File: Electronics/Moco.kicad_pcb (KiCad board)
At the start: 2 copper layers, 34 x 34 mm, 51 parts, among them J1 Conn_01x04, J2 Conn_01x01, J3 Conn_ARM_JTAG_SWD_10, J4 Conn_01x03, J5 Conn_01x01, J6 Conn_01x04, J8 Conn_01x01, J9 Conn_01x01, U1 EFM32PG22C200FxxIM32, U2 SP485EN, U3 TMAG5273, U4 DRV8311, Y1 ECS-384-CDX-1983

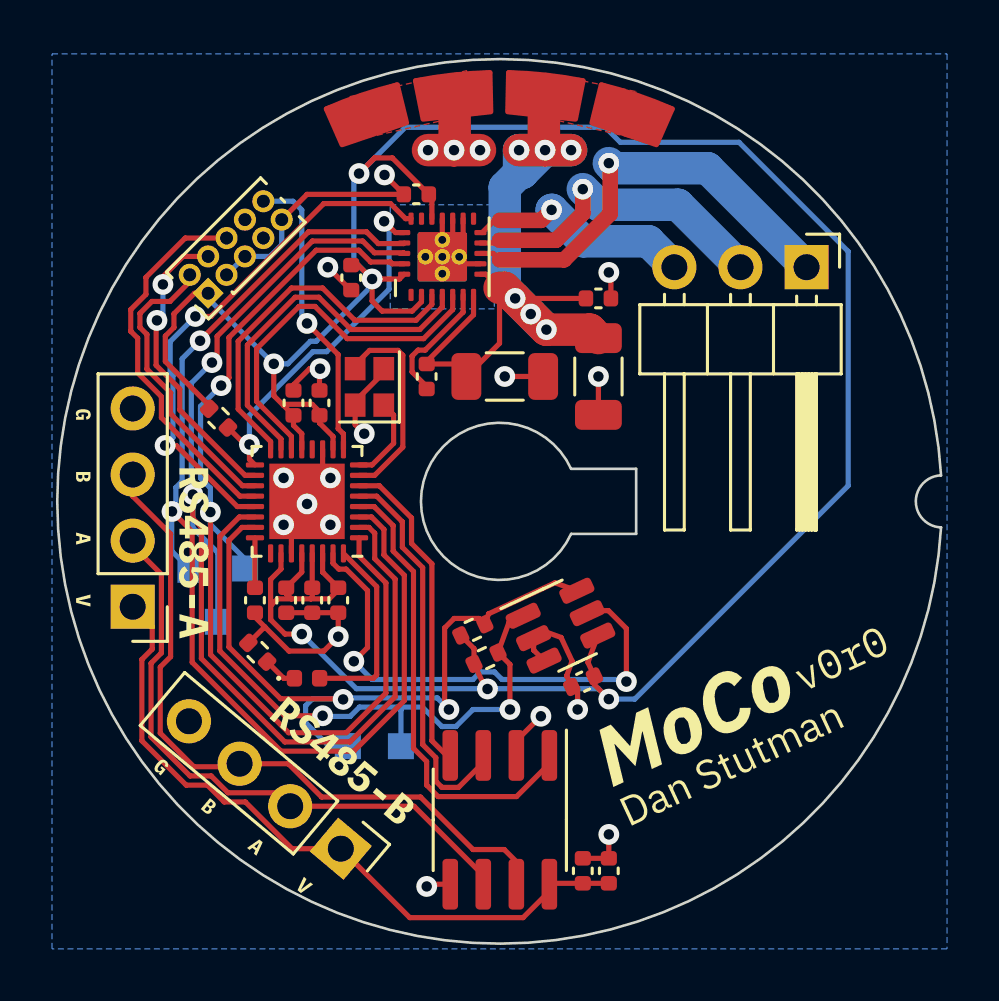
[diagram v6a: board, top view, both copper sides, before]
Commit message: New design with ESP32-C3
This design swaps the EFM32PG22 for an ESP32-C3. This reduces cost
and improves availability. It also lets me use USB and CANbus instead
of RS485.
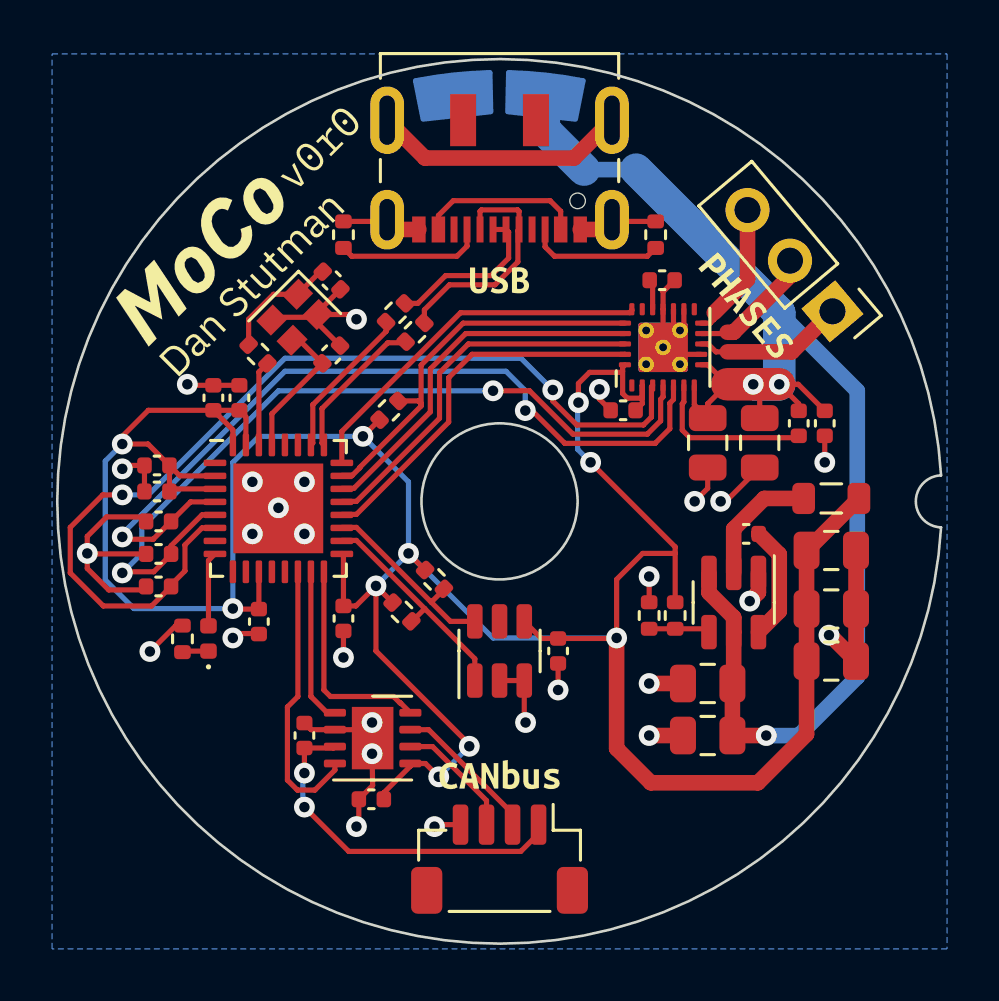
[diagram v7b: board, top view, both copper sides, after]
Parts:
- removed C16: 0.1 + 2.7 uF 6.3V X5R, Capacitor_SMD:C_0402_1005Metric
- removed C2, C3: 0.1 uF 6.3V X5R, Capacitor_SMD:C_0402_1005Metric
- removed C4: 0.1 + 1 uF 6.3V X5R, Capacitor_SMD:C_0402_1005Metric
- removed C6: 0.01 + 1 uF 6.3V X5R, Capacitor_SMD:C_0402_1005Metric
- removed J1: Conn_01x04, Connector_PinHeader_2.54mm:PinHeader_1x04_P2.54mm_Vertical
- removed J2, J5: Conn_01x01, Library:Pad_CircularEdge_Ro16.5Ri15_Single
- removed TP1, TP2, TP3, TP4, TP5: TestPoint, TestPoint:TestPoint_Pad_1.0x1.0mm
- removed kibuzzard-624C45BD: G***, kibuzzard-624C45BD
- removed kibuzzard-624C45C7: G***, kibuzzard-624C45C7
- removed kibuzzard-624C45D0: G***, kibuzzard-624C45D0
- removed kibuzzard-624C45D8: G***, kibuzzard-624C45D8
- removed kibuzzard-624C45E2: G***, kibuzzard-624C45E2
- removed kibuzzard-6257E5BB: G***, kibuzzard-6257E5BB
- removed kibuzzard-6257E5C8: G***, kibuzzard-6257E5C8
- removed kibuzzard-6257E666 (x2): G***, kibuzzard-6257E666
- added C14: C_Small, Capacitor_SMD:C_0402_1005Metric, F.Cu at (36.9, 50.8)
- added C17: C_Small, Capacitor_SMD:C_0402_1005Metric, F.Cu at (36.9, 52.0)
- added C18: C_Small, Capacitor_SMD:C_0402_1005Metric, F.Cu at (40.0, 46.0)
- added C19: C_Small, Capacitor_SMD:C_0402_1005Metric, F.Cu at (43.5, 44.4)
- added C20: C_Small, Capacitor_SMD:C_0402_1005Metric, F.Cu at (43.5, 41.5)
- added C21: C_Small, Capacitor_SMD:C_0402_1005Metric, F.Cu at (36.8, 48.6)
- added C22: C_Small, Capacitor_SMD:C_0402_1005Metric, F.Cu at (36.8, 49.6)
- added C23: C_Small, Capacitor_SMD:C_0402_1005Metric, F.Cu at (40.8, 54.6)
- added C24: C_Small, Capacitor_SMD:C_0402_1005Metric, F.Cu at (44.0, 54.5)
- added C25: C_Small, Capacitor_SMD:C_0402_1005Metric, F.Cu at (36.9, 53.3)
- added C26: 10uF, Capacitor_SMD:C_0805_2012Metric, F.Cu at (58.0, 57.0)
- added C27: 10uF, Capacitor_SMD:C_0805_2012Metric, F.Cu at (58.0, 59.0)
- added C28: 0.1uF, Capacitor_SMD:C_0402_1005Metric, F.Cu at (59.5, 51.2)
- added C29: 22uF, Capacitor_SMD:C_0805_2012Metric, F.Cu at (62.8, 51.9)
- added C30: 22uF, Capacitor_SMD:C_0805_2012Metric, F.Cu at (62.8, 54.1)
- added C31: 22uF, Capacitor_SMD:C_0805_2012Metric, F.Cu at (62.8, 56.1)
- added L2: 3.3uH 114mR, Inductor_SMD:L_0805_2012Metric, F.Cu at (62.8, 49.9)
- added R10: 22R, Resistor_SMD:R_0402_1005Metric, F.Cu at (46.8, 43.5)
- added R11: 22R, Resistor_SMD:R_0402_1005Metric, F.Cu at (46.0, 42.8)
- added R5: R_Small_US, Resistor_SMD:R_0402_1005Metric, F.Cu at (40.7, 44.3)
- added R6: 33.2kR, Resistor_SMD:R_0402_1005Metric, F.Cu at (56.8, 54.4)
- added R7: 10kR, Resistor_SMD:R_0402_1005Metric, F.Cu at (55.8, 54.4)
- added R8: 5.1kR, Resistor_SMD:R_0402_1005Metric, F.Cu at (56.0, 39.8)
- added R9: 5.1kR, Resistor_SMD:R_0402_1005Metric, F.Cu at (44.0, 39.8)
- added U5: TJA1462ATK/0Z, Package_SON:HVSON-8-1EP_3x3mm_P0.65mm_EP1.6x2.4mm, F.Cu at (45.1, 59.1)
- added kibuzzard-626ED451: G***, kibuzzard-626ED451, F.Cu at (50.0, 60.5)
- added kibuzzard-626ED465: G***, kibuzzard-626ED465, F.Cu at (50.0, 41.5)
- added kibuzzard-626ED487: G***, kibuzzard-626ED487, F.Cu at (59.5, 42.5)
- C1: value 1 uF 6.3V X5R -> C_Small
- C12: value 1uF 6.3V X7R -> 0.1uF 6.3V X7R
- C13, C15: footprint Capacitor_SMD:C_1206_3216Metric -> Capacitor_SMD:C_0805_2012Metric
- J3: value Conn_ARM_JTAG_SWD_10 -> USB_C_Receptacle_USB2.0; footprint Connector_PinHeader_1.00mm:PinHeader_2x05_P1.00mm_Vertical -> Connector_USB:USB_C_Receptacle_JAE_DX07S016JA1R1500
- J4: footprint Connector_PinHeader_2.54mm:PinHeader_1x03_P2.54mm_Horizontal -> Connector_PinHeader_2.54mm:PinHeader_1x03_P2.54mm_Vertical
- J6: footprint Connector_PinHeader_2.54mm:PinHeader_1x04_P2.54mm_Vertical -> Connector_JST:JST_SH_BM04B-SRSS-TB_1x04-1MP_P1.00mm_Vertical
- J8, J9: moved to B.Cu
- R1, R2: value 910kR -> 910R
- U1: value EFM32PG22C200FxxIM32 -> ESP32-C3; footprint Package_DFN_QFN:QFN-32-1EP_4x4mm_P0.4mm_EP2.9x2.9mm -> Package_DFN_QFN:QFN-32-1EP_5x5mm_P0.5mm_EP3.45x3.45mm
- U2: value SP485EN -> TPS562201; footprint Package_SO:SOIC-8_3.9x4.9mm_P1.27mm -> Package_TO_SOT_SMD:SOT-23-6
- Y1: value ECS-384-CDX-1983 -> XTAL
- moved kibuzzard-624C491C 28.1 mm to (43.1, 36.4), turned to 45 degrees
- moved kibuzzard-6244D452 26.1 mm to (40.5, 41.6), turned to 45 degrees
- moved kibuzzard-6244CA09 26.0 mm to (38.5, 40.5), turned to 45 degrees
- moved C8 14.4 mm to (61.5, 47.0)
- moved J3 12.5 mm to (50.0, 36.5), turned to 180 degrees
- moved U2 12.3 mm to (59.0, 53.9)
- moved C5 11.9 mm to (42.5, 59.0)
- moved C7 11.6 mm to (54.8, 46.5), turned to 0 degrees
- moved C10 10.0 mm to (56.2, 41.5), turned to 0 degrees
- moved C11 9.94 mm to (62.5, 47.0), turned to -90 degrees
- moved C12 9.53 mm to (45.1, 61.5), turned to 180 degrees
- moved U4 9.17 mm to (56.3, 44.1)
- moved C15 8.21 mm to (58.0, 47.8), turned to -90 degrees
- moved C1 7.94 mm to (39.0, 46.0)
- moved C13 6.70 mm to (60.0, 47.8)
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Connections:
- C1 pad 1: GND -> +3V3
- C1 pad 2: Net-(C1-Pad2) -> GND
- C10 pad 1: +3V3 -> Net-(C10-Pad1)
- C12 pad 1: +5V -> +3V3
- J6 pad 2: /RS485_A -> /CANH
- J6 pad 3: /RS485_B -> /CANL
- U1 pad 1: /SCLK -> unconnected-(U1-Pad1)
- U1 pad 10: +3V3 -> unconnected-(U1-Pad10)
- U1 pad 11: GND -> +3V3
- U1 pad 13: +3V3 -> unconnected-(U1-Pad13)
- U1 pad 14: /SOA -> /CAN_RX
- U1 pad 15: /SOB -> /CAN_TX
- U1 pad 16: /SOC -> /CAN_EN
- U1 pad 17: /DRV_~{SCS} -> +3V3
- U1 pad 18: /SWCLK -> /TMS_SDA
- U1 pad 19: /SWDIO -> /TMS_SCL
- U1 pad 2: /SDI -> +3V3
- U1 pad 20: /SWO -> /SCLK
- U1 pad 21: /PWM_SYNC -> /SDI
- U1 pad 22: /TMS_SDA -> /SDO
- U1 pad 23: /TMS_SCL -> /DRV_~{SCS}
- U1 pad 24: Net-(C1-Pad2) -> /PWM_SYNC
- U1 pad 25: unconnected-(U1-Pad25) -> /USB_DN
- U1 pad 26: +3V3 -> /USB_DP
- U1 pad 27: GND -> unconnected-(U1-Pad27)
- U1 pad 28: +3V3 -> unconnected-(U1-Pad28)
- U1 pad 29: +3V3 -> Net-(C19-Pad1)
- U1 pad 3: /SDO -> +3V3
- U1 pad 30: +3V3 -> Net-(R5-Pad2)
- U1 pad 31: /~{INT} -> +3V3
- U1 pad 32: Net-(D1-Pad2) -> +3V3
- U1 pad 4: /UART_RX -> /SOA
- U1 pad 5: /UART_CS -> /SOB
- U1 pad 6: /UART_TX -> /SOC
- U1 pad 7: Net-(U1-Pad7) -> /~{RESET}
- U1 pad 8: Net-(U1-Pad8) -> Net-(D1-Pad2)
- U1 pad 9: /~{RESET} -> unconnected-(U1-Pad9)
- U2 pad 1: /UART_RX -> GND
- U2 pad 2: GND -> Net-(C28-Pad1)
- U2 pad 3: /UART_CS -> Vdrive
- U2 pad 4: /UART_TX -> Net-(R6-Pad2)
- U2 pad 5: GND -> Vdrive
- U2 pad 6: /RS485_A -> Net-(C28-Pad2)
- U3 pad 5: /~{INT} -> unconnected-(U3-Pad5)
- U4 pad 17: +3V3 -> Net-(C10-Pad1)
- Y1 pad 1: Net-(U1-Pad8) -> Net-(C20-Pad1)
- Y1 pad 3: Net-(U1-Pad7) -> Net-(C19-Pad1)
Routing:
- net /SDO: track 43.9 -> 14.3 mm, vias 2 -> 0
- net /SDI: track 44.0 -> 14.4 mm, vias 2 -> 0
- net /RS485_B: track 26.4 -> 0.00 mm
- net GND: track 47.7 -> 72.7 mm, vias 20 -> 27
- net /SCLK: track 38.9 -> 14.4 mm, vias 2 -> 0
- net Vdrive: track 32.7 -> 56.2 mm, vias 6 -> 3
- net /SOC: track 14.1 -> 37.4 mm, vias 0 -> 2
- net /RS485_A: track 22.2 -> 0.00 mm
- net /TMS_SCL: track 28.2 -> 7.32 mm, vias 2 -> 0
- net /~{INT}: track 19.8 -> 0.00 mm, vias 2 -> 0
- net /UART_RX: track 17.5 -> 0.00 mm
- net /SOA: track 14.2 -> 31.5 mm, vias 0 -> 2
- net /SOB: track 14.1 -> 31.2 mm, vias 0 -> 2
- net /TMS_SDA: track 24.7 -> 8.55 mm, vias 2 -> 0
- net /UART_CS: track 14.9 -> 0.00 mm
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- removed copper zone on F.Cu, net GND
- removed copper zone on F.Cu, net Vdrive
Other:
- outline, holes or cut-outs redrawn

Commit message: Complete ESP32-C3 redesign
- Remove status LED to free up pin
- Avoid using embedded flash SPI pins
- Update silkscreen
- Improve I2C and CANbus pin assignments
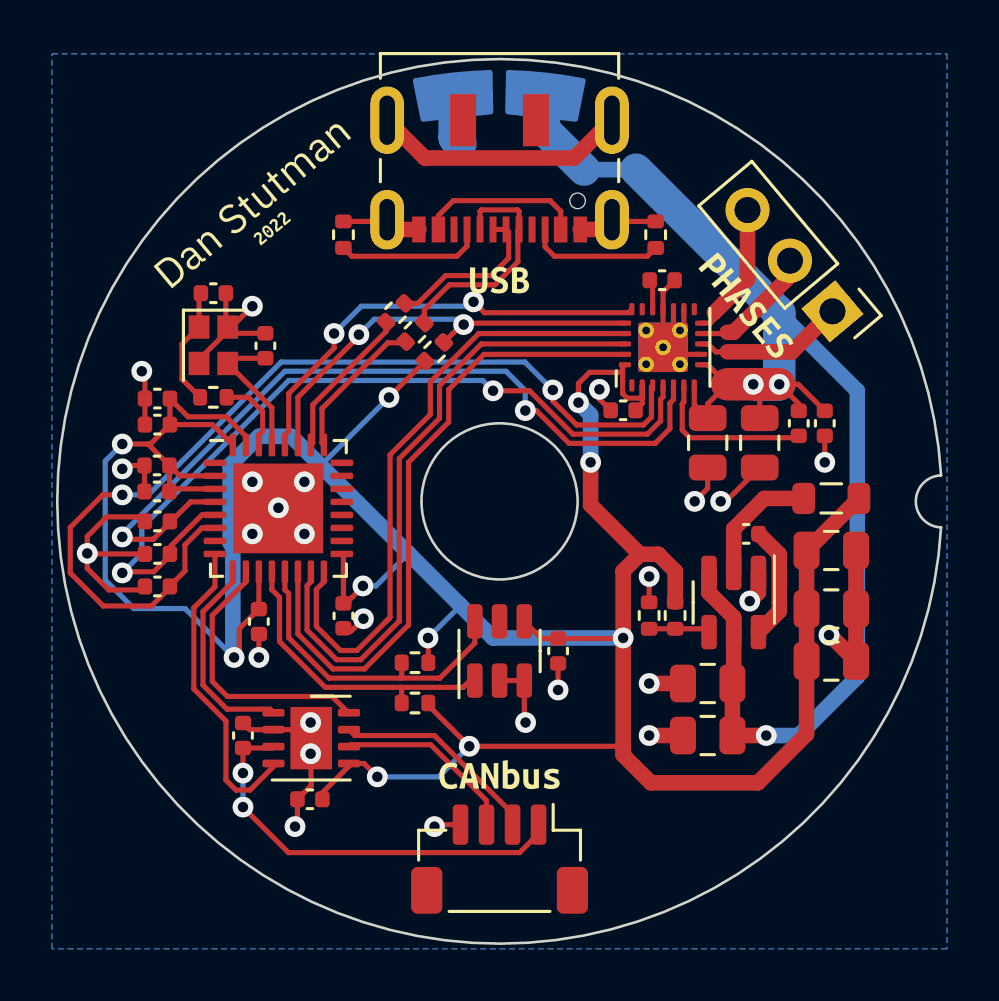
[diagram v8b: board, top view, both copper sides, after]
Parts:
- removed D1: LED, LED_SMD:LED_0402_1005Metric
- removed R3: R_Small_US, Resistor_SMD:R_0402_1005Metric
- added kibuzzard-62725C85: G***, kibuzzard-62725C85, F.Cu at (41.2, 39.5)
- C1: value C_Small -> 1uF 6.3V
- C10: value 1uF 6.3V X7R -> 1uF 6.3V
- C11: value 0.1uF VBUS X7R -> 0.1uF VBUS
- C12, C9: value 0.1uF 6.3V X7R -> 0.1uF 6.3V
- C13, C15: value 10uF VBUS X7R -> 10uF VBUS
- C14, C17, C21, C22, C23, C24, C25: value C_Small -> 0.1uF 6.3V
- C18: value C_Small -> 10nF 6.3V
- C19, C20: value C_Small -> XpF 6.3V
- C26, C27: value 10uF -> 10uF 25V
- C29, C30, C31: value 22uF -> 22uF 6.3V
- C5: value 0.1uF 6.3V X7R -> 0.1uF 10V
- C8: value 0.1uF 16V X7R -> 0.1uF 25V
- L2: value 3.3uH 114mR -> 3.3uH 750mA
- R5: value R_Small_US -> 100R
- Y1: value XTAL -> 40 MHz +-10ppm
- kibuzzard-6244CA09, kibuzzard-624C491C: moved to B.Cu
- moved kibuzzard-624C491C 15.9 mm to (40.0, 52.0), turned to 180 degrees
- moved kibuzzard-6244CA09 9.66 mm to (40.2, 50.0), turned to 180 degrees
- moved C20 4.57 mm to (39.0, 42.0), turned to 0 degrees
- moved R2 3.54 mm to (46.8, 57.8), turned to 180 degrees
- moved Y1 3.31 mm to (39.0, 44.0), turned to -90 degrees
- moved R1 3.29 mm to (46.8, 56.2), turned to 0 degrees
- moved C18 3.15 mm to (36.9, 46.0), turned to 180 degrees
- moved kibuzzard-6244D452 3.13 mm to (40.5, 38.5), turned to 40 degrees
- moved R4 2.85 mm to (47.5, 44.2)
- moved C19 2.55 mm to (41.0, 44.0), turned to 90 degrees
- moved R5 2.39 mm to (39.0, 46.0), turned to 0 degrees
- moved C1 2.38 mm to (36.9, 47.0), turned to 180 degrees
- moved U5 2.36 mm to (42.8, 59.1)
- moved C12 2.36 mm to (42.7, 61.5)
- moved C5 2.36 mm to (40.1, 59.0)
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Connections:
- U1 pad 10: unconnected-(U1-Pad10) -> /CAN_EN
- U1 pad 12: unconnected-(U1-Pad12) -> /TMS_SDA
- U1 pad 13: unconnected-(U1-Pad13) -> /TMS_SCL
- U1 pad 14: /CAN_RX -> /SCLK
- U1 pad 15: /CAN_TX -> /SDI
- U1 pad 16: /CAN_EN -> /SDO
- U1 pad 18: /TMS_SDA -> unconnected-(U1-Pad18)
- U1 pad 19: /TMS_SCL -> unconnected-(U1-Pad19)
- U1 pad 20: /SCLK -> unconnected-(U1-Pad20)
- U1 pad 21: /SDI -> unconnected-(U1-Pad21)
- U1 pad 22: /SDO -> unconnected-(U1-Pad22)
- U1 pad 23: /DRV_~{SCS} -> unconnected-(U1-Pad23)
- U1 pad 24: /PWM_SYNC -> unconnected-(U1-Pad24)
- U1 pad 27: unconnected-(U1-Pad27) -> /DRV_~{SCS}
- U1 pad 28: unconnected-(U1-Pad28) -> /PWM_SYNC
- U1 pad 8: Net-(D1-Pad2) -> /CAN_RX
- U1 pad 9: unconnected-(U1-Pad9) -> /CAN_TX
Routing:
- net +3V3: track 121.5 -> 132.1 mm
- net /SCLK: track 14.4 -> 24.9 mm
- net /SDI: track 14.4 -> 24.4 mm
- net /SDO: track 14.3 -> 24.1 mm
- net /TMS_SCL: track 7.32 -> 12.4 mm
- net /TMS_SDA: track 8.55 -> 11.8 mm
- net /PWM_SYNC: track 14.3 -> 17.2 mm, vias 0 -> 2
- net Net-(D1-Pad2): track 2.87 -> 0.00 mm
- net /CANH: track 5.69 -> 8.47 mm
- net /CANL: track 4.71 -> 7.13 mm
- net +5V: track 13.9 -> 16.2 mm
- net /CAN_EN: track 8.25 -> 10.5 mm
- net /CAN_TX: track 5.99 -> 7.98 mm
- net /DRV_~{SCS}: track 15.2 -> 16.8 mm, vias 0 -> 2
- net /CAN_RX: track 10.7 -> 12.0 mm
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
